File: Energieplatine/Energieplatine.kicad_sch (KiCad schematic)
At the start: 39 parts, among them J1 USB_C_Receptacle_PowerOnly_6P, J2 Conn_01x02_Pin, J3 Conn_01x02_Pin, J4 Conn_02x07_Odd_Even, J5 Conn_01x02_Pin, J6 Conn_01x02_Pin, Q1 IRF9540N, Q2 IRF9540N, Q3 IRF540N, U1 4027, U2 TL072, U3 LM2576HVT-ADJ, U4 LM2577T-ADJ

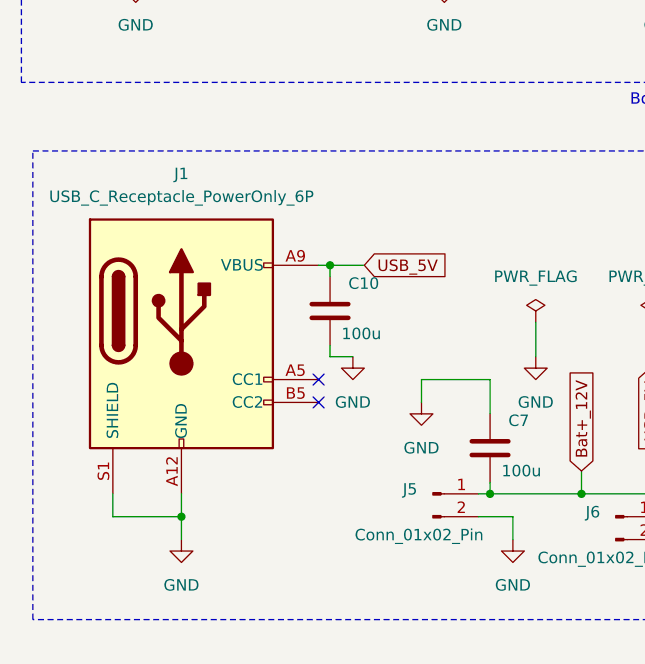
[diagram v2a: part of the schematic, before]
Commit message: added usb-typeA
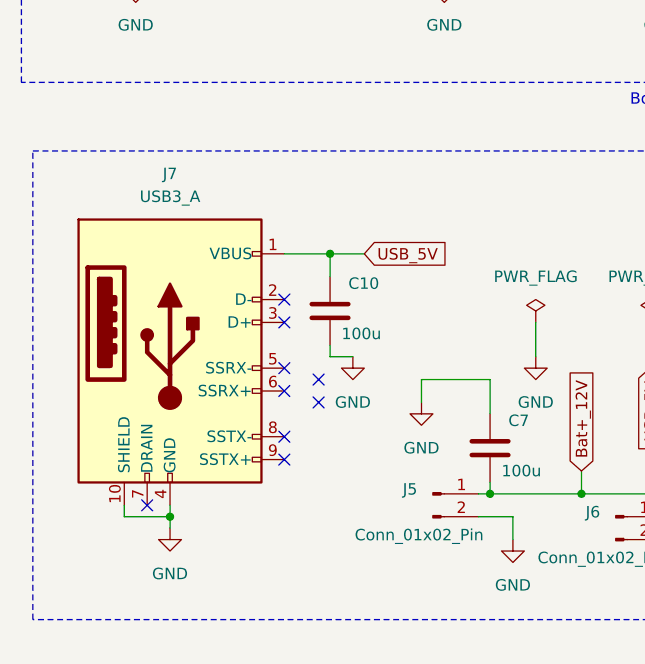
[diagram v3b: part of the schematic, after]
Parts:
- removed J1: USB_C_Receptacle_PowerOnly_6P, Connector_USB:USB_C_Receptacle_GCT_USB4125-xx-x-0190_6P_TopMnt_Horizontal, symbol Connector:USB_C_Receptacle_PowerOnly_6P
- added J7: USB3_A, Projektlabor:USB3_A_Molex_48393-001_short, symbol Connector:USB3_A
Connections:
- net GND: now also J7.10 (SHIELD), J7.4 (GND)
- net USB_5V: now also J7.1 (VBUS)
- no-connect marks 18 -> 25
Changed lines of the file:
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@@
 	)
 	(junction
+		(at 31.75 180.34)
+		(diameter 0)
+		(color 0 0 0 0)
+	)
+	(junction
 		(at 224.79 100.33)
 		(diameter 0)
@@
 	)
 	(junction
-		(at 49.53 152.4)
+		(at 49.53 151.13)
 		(diameter 0)
 		(color 0 0 0 0)
@@
 		(color 0 0 0 0)
 	)
-	(junction
-		(at 33.02 180.34)
-		(diameter 0)
-		(color 0 0 0 0)
-	)
 	(no_connect
 		(at 181.61 113.03)
@@
 	)
 	(no_connect
+		(at 44.45 173.99)
+	)
+	(no_connect
 		(at 168.91 118.11)
 	)
@@
 	)
 	(no_connect
+		(at 44.45 163.83)
+	)
+	(no_connect
+		(at 44.45 166.37)
+	)
+	(no_connect
 		(at 26.67 24.13)
 	)
@@
 	)
 	(no_connect
+		(at 44.45 171.45)
+	)
+	(no_connect
+		(at 44.45 158.75)
+	)
+	(no_connect
+		(at 29.21 179.07)
+	)
+	(no_connect
 		(at 168.91 110.49)
 	)
@@
 	)
 	(no_connect
+		(at 44.45 156.21)
+	)
+	(no_connect
 		(at 168.91 113.03)
 	)
@@
 	(wire
 		(pts
+			(xy 31.75 179.07) (xy 31.75 180.34)
+		)
+		(stroke
+			(width 0)
+			(type default)
+		)
+	)
+	(wire
+		(pts
+			(xy 31.75 180.34) (xy 31.75 181.61)
+		)
+		(stroke
+			(width 0)
+			(type default)
+		)
+	)
+	(wire
+		(pts
 			(xy 52.07 26.67) (xy 55.88 26.67)
 		)
@@
 	(wire
 		(pts
+			(xy 26.67 179.07) (xy 26.67 180.34)
+		)
+		(stroke
+			(width 0)
+			(type default)
+		)
+	)
+	(wire
+		(pts
 			(xy 121.92 33.02) (xy 128.27 33.02)
 		)
@@
 	(wire
 		(pts
-			(xy 49.53 152.4) (xy 49.53 153.67)
+			(xy 66.04 177.8) (xy 67.31 177.8)
 		)
 		(stroke
@@
 	(wire
 		(pts
-			(xy 66.04 177.8) (xy 67.31 177.8)
+			(xy 96.52 90.17) (xy 100.33 90.17)
 		)
 		(stroke
@@
 	(wire
 		(pts
-			(xy 96.52 90.17) (xy 100.33 90.17)
+			(xy 109.22 31.75) (xy 109.22 34.29)
 		)
 		(stroke
@@
 	(wire
 		(pts
-			(xy 109.22 31.75) (xy 109.22 34.29)
+			(xy 53.34 44.45) (xy 53.34 45.72)
 		)
 		(stroke
@@
 	(wire
 		(pts
-			(xy 53.34 44.45) (xy 53.34 45.72)
+			(xy 74.93 109.22) (xy 86.36 109.22)
 		)
 		(stroke
@@
 	(wire
 		(pts
-			(xy 74.93 109.22) (xy 86.36 109.22)
+			(xy 180.34 43.18) (xy 180.34 44.45)
 		)
 		(stroke
@@
 	(wire
 		(pts
-			(xy 180.34 43.18) (xy 180.34 44.45)
+			(xy 49.53 151.13) (xy 53.34 151.13)
 		)
 		(stroke
@@
 	(wire
 		(pts
+			(xy 49.53 151.13) (xy 49.53 153.67)
+		)
+		(stroke
+			(width 0)
+			(type default)
+		)
+	)
+	(wire
+		(pts
 			(xy 193.04 33.02) (xy 205.74 33.02)
 		)
@@
 	(wire
 		(pts
-			(xy 48.26 152.4) (xy 49.53 152.4)
-		)
-		(stroke
-			(width 0)
-			(type default)
-		)
-	)
-	(wire
-		(pts
 			(xy 241.3 53.34) (xy 224.79 53.34)
 		)
@@
 	(wire
 		(pts
-			(xy 25.4 180.34) (xy 33.02 180.34)
-		)
-		(stroke
-			(width 0)
-			(type default)
-		)
-	)
-	(wire
-		(pts
 			(xy 78.74 26.67) (xy 78.74 27.94)
 		)
@@
 	(wire
 		(pts
-			(xy 49.53 152.4) (xy 53.34 152.4)
+			(xy 58.42 31.75) (xy 55.88 31.75)
 		)
 		(stroke
@@
 	(wire
 		(pts
-			(xy 58.42 31.75) (xy 55.88 31.75)
+			(xy 241.3 41.91) (xy 241.3 53.34)
 		)
 		(stroke
@@
 	(wire
 		(pts
-			(xy 241.3 41.91) (xy 241.3 53.34)
+			(xy 274.32 101.6) (xy 274.32 97.79)
 		)
 		(stroke
@@
 	(wire
 		(pts
-			(xy 274.32 101.6) (xy 274.32 97.79)
+			(xy 44.45 151.13) (xy 49.53 151.13)
 		)
 		(stroke
@@
 	(wire
 		(pts
-			(xy 25.4 177.8) (xy 25.4 180.34)
+			(xy 26.67 180.34) (xy 31.75 180.34)
 		)
 		(stroke
@@
 	(wire
 		(pts
-			(xy 33.02 180.34) (xy 33.02 182.88)
-		)
-		(stroke
-			(width 0)
-			(type default)
-		)
-	)
-	(wire
-		(pts
 			(xy 49.53 161.29) (xy 49.53 162.56)
 		)
@@
 	(wire
 		(pts
-			(xy 33.02 180.34) (xy 33.02 177.8)
-		)
-		(stroke
-			(width 0)
-			(type default)
-		)
-	)
-	(wire
-		(pts
 			(xy 53.34 44.45) (xy 58.42 44.45)
 		)
@@
 	(global_label "USB_5V"
 		(shape input)
-		(at 53.34 152.4 0)
+		(at 53.34 151.13 0)
 		(fields_autoplaced yes)
 		(effects
@@
 		)
 		(property "Intersheetrefs" "${INTERSHEET_REFS}"
-			(at 63.4009 152.4 0)
+			(at 63.4009 151.13 0)
 			(effects
 				(font
@@
 	(symbol
 		(lib_id "power:GND")
-		(at 33.02 182.88 0)
+		(at 31.75 181.61 0)
 		(unit 1)
 		(exclude_from_sim no)
@@
 		(fields_autoplaced yes)
 		(property "Reference" "#PWR01"
-			(at 33.02 189.23 0)
+			(at 31.75 187.96 0)
 			(effects
 				(font
@@
 		)
 		(property "Value" "GND"
-			(at 33.02 187.96 0)
+			(at 31.75 186.69 0)
 			(effects
 				(font
@@
 		)
 		(property "Footprint" ""
-			(at 33.02 182.88 0)
+			(at 31.75 181.61 0)
 			(effects
 				(font
@@
 		)
 		(property "Datasheet" ""
-			(at 33.02 182.88 0)
+			(at 31.75 181.61 0)
 			(effects
 				(font
@@
 		)
 		(property "Description" "Power symbol creates a global label with name \"GND\" , ground"
-			(at 33.02 182.88 0)
+			(at 31.75 181.61 0)
 			(effects
 				(font
@@
 	)
 	(symbol
-		(lib_id "Connector:USB_C_Receptacle_PowerOnly_6P")
-		(at 33.02 160.02 0)
-		(unit 1)
-		(exclude_from_sim no)
-		(in_bom yes)
-		(on_board yes)
-		(dnp no)
-		(fields_autoplaced yes)
-		(property "Reference" "J1"
-			(at 33.02 142.24 0)
-			(effects
-				(font
-					(size 1.27 1.27)
-				)
-			)
-		)
-		(property "Value" "USB_C_Receptacle_PowerOnly_6P"
-			(at 33.02 144.78 0)
-			(effects
-				(font
-					(size 1.27 1.27)
-				)
-			)
-		)
-		(property "Footprint" "Connector_USB:USB_C_Receptacle_GCT_USB4125-xx-x-0190_6P_TopMnt_Horizontal"
-			(at 36.83 157.48 0)
-			(effects
-				(font
-					(size 1.27 1.27)
-				)
-				(hide yes)
-			)
-		)
-		(property "Datasheet" "https://www.usb.org/sites/default/files/documents/usb_type-c.zip"
-			(at 33.02 160.02 0)
-			(effects
-				(font
-					(size 1.27 1.27)
-				)
-				(hide yes)
-			)
-		)
-		(property "Description" "USB Power-Only 6P Type-C Receptacle connector"
-			(at 33.02 160.02 0)
-			(effects
-				(font
-					(size 1.27 1.27)
-				)
-				(hide yes)
-			)
-		)
-		(pin "A5"
-		)
-		(pin "B5"
-		)
-		(pin "A12"
-		)
-		(pin "A9"
-		)
-		(pin "S1"
-		)
-		(pin "B9"
-		)
-		(pin "B12"
-		)
-		(instances
-			(project "Energieplatine"
-				(path "/03a54101-e95a-4ac4-b362-52e71af40d1b"
-					(reference "J1")
-					(unit 1)
-				)
-			)
-		)
-	)
-	(symbol
 		(lib_id "power:PWR_FLAG")
 		(at 97.79 158.75 0)
@@
 					(unit 1)
 				)
+			)
+		)
+	)
+	(symbol
+		(lib_id "Connector:USB3_A")
+		(at 31.75 161.29 0)
+		(unit 1)
+		(exclude_from_sim no)
+		(in_bom yes)
+		(on_board yes)
+		(dnp no)
+		(fields_autoplaced yes)
+		(property "Reference" "J7"
+			(at 31.75 142.24 0)
+			(effects
+				(font
+					(size 1.27 1.27)
+				)
+			)
+		)
+		(property "Value" "USB3_A"
+			(at 31.75 144.78 0)
+			(effects
+				(font
+					(size 1.27 1.27)
+				)
+			)
+		)
+		(property "Footprint" "Projektlabor:USB3_A_Molex_48393-001_short"
+			(at 35.56 158.75 0)
+			(effects
+				(font
+					(size 1.27 1.27)
+				)
+				(hide yes)
+			)
+		)
+		(property "Datasheet" "~"
+			(at 35.56 158.75 0)
+			(effects
+				(font
+					(size 1.27 1.27)
+				)
+				(hide yes)
+			)
+		)
+		(property "Description" "USB 3.0 A connector"
+			(at 31.75 161.29 0)
+			(effects
+				(font
+					(size 1.27 1.27)
+				)
+				(hide yes)
+			)
+		)
+		(pin "3"
+		)
+		(pin "5"
+		)
+		(pin "2"
+		)
+		(pin "1"
+		)
+		(pin "8"
+		)
+		(pin "7"
+		)
+		(pin "10"
+		)
+		(pin "9"
+		)
+		(pin "4"
+		)
+		(pin "6"
+		)
+		(instances
+			(project "Energieplatine"
+				(path "/03a54101-e95a-4ac4-b362-52e71af40d1b"
+					(reference "J7")
+					(unit 1)
+				)
